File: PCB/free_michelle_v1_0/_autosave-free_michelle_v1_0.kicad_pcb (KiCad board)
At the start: 2 copper layers, 101 parts, among them J1 Zworka_TX, J10 ARK, J11 ARK, J12 Zworka_Buzzer, J13 ARK, J14 ARK, J15 Gniazdo 5VP DC 5,5x2,5, J16 Gniazdo 9V DC 5,5x2,5, J2 Zworka_RX, J3 GROVE_SW, J4 ARK, J5 ARK, J6 ARK, J7 ARK, J8 GROVE_SW, J9 A02YYUW_GroveCON, K1 FINDER-36.11, K2 FINDER-36.11, K3 FINDER-36.11, K4 FINDER-36.11, K5 FINDER-36.11, K6 FINDER-36.11, K7 FINDER-36.11, K8 FINDER-36.11, Q1 MMBT4403_PNP, Q2 MMBT4403_PNP, Q3 MMBT4403_PNP, Q4 MMBT4403_PNP, Q5 BSS138, Q6 MMBT4403_PNP, Q7 MMBT4403_PNP, Q8 MMBT4403_PNP, Q9 MMBT4403_PNP, SW1 Rotary_Encoder, SW2 SW_Push, SW3 SW_Push, U1 EEPROM_24AA01, U2 ESP8266_NodeMCU_v2, U3 DS3231M_RTC, U4 NRF24L01_Breakout, U5 BMP280, U6 LD1117V33, U7 L7805, U8 LD1117V33

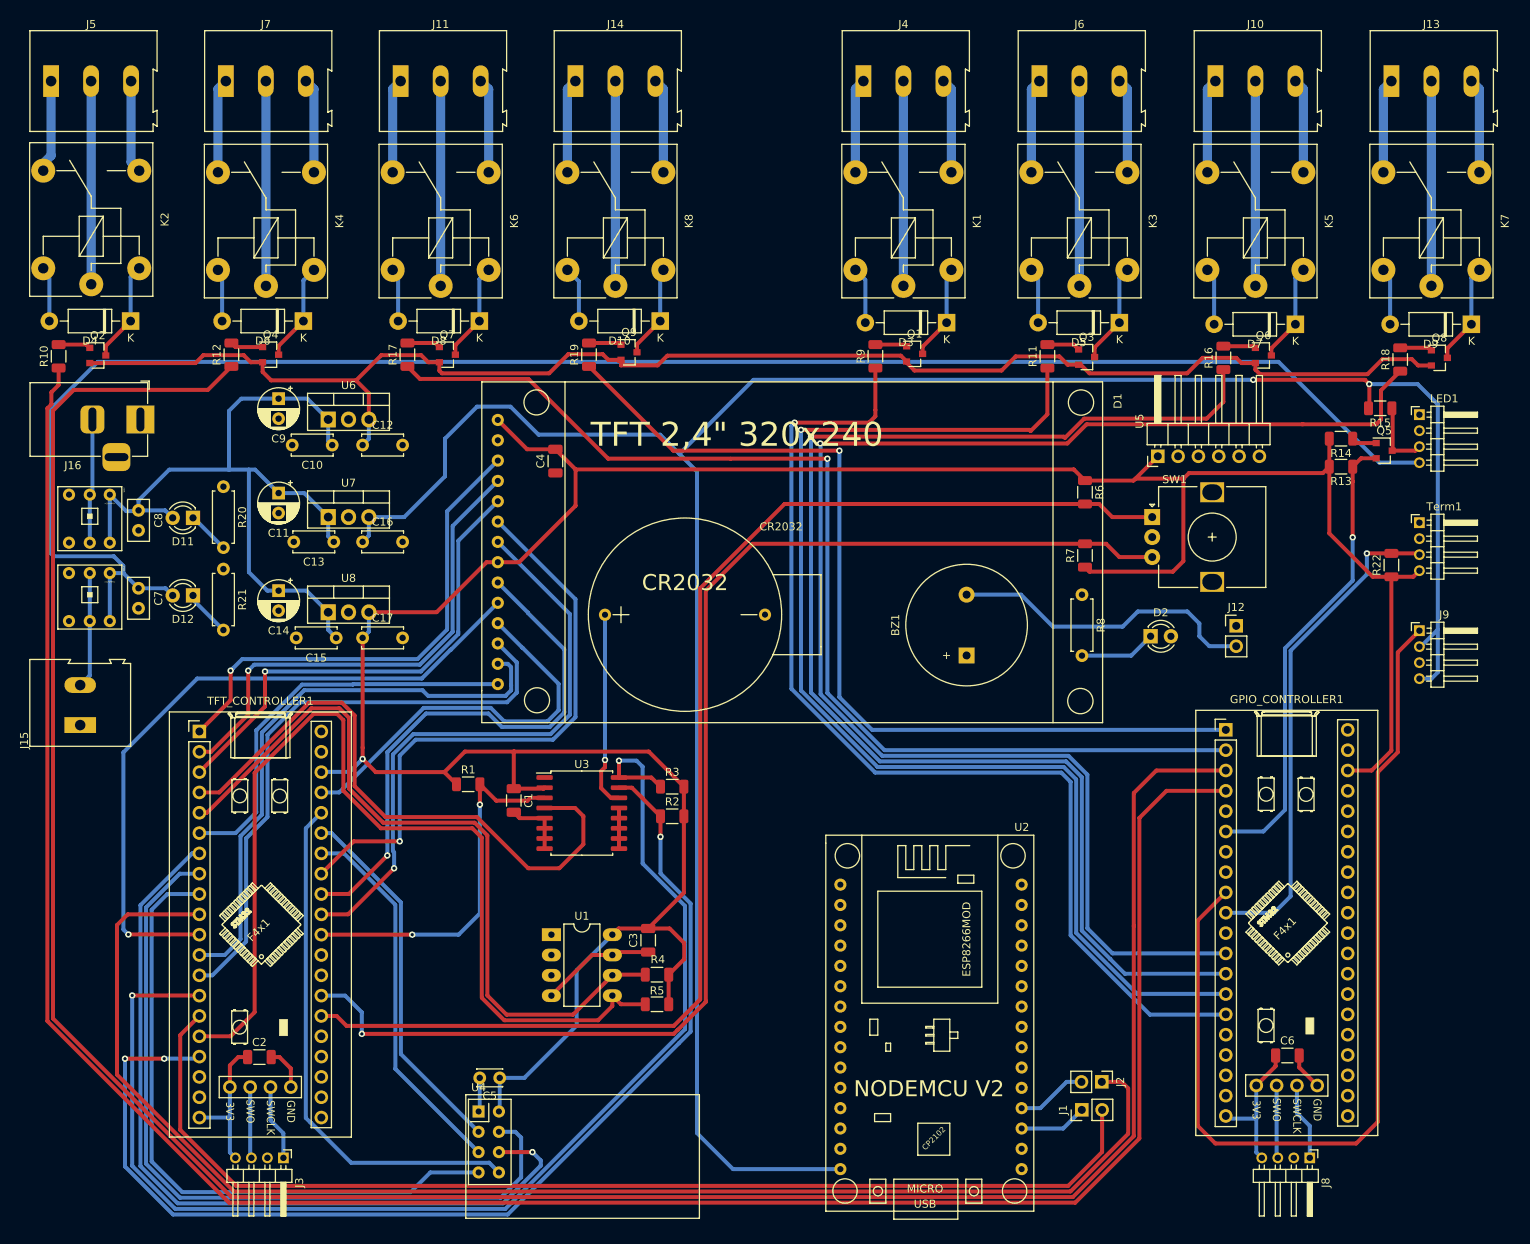
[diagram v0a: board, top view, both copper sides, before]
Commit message: Wykonane wszystkie polaczenia sygnalowe i zasilania, przed wylaniem masy
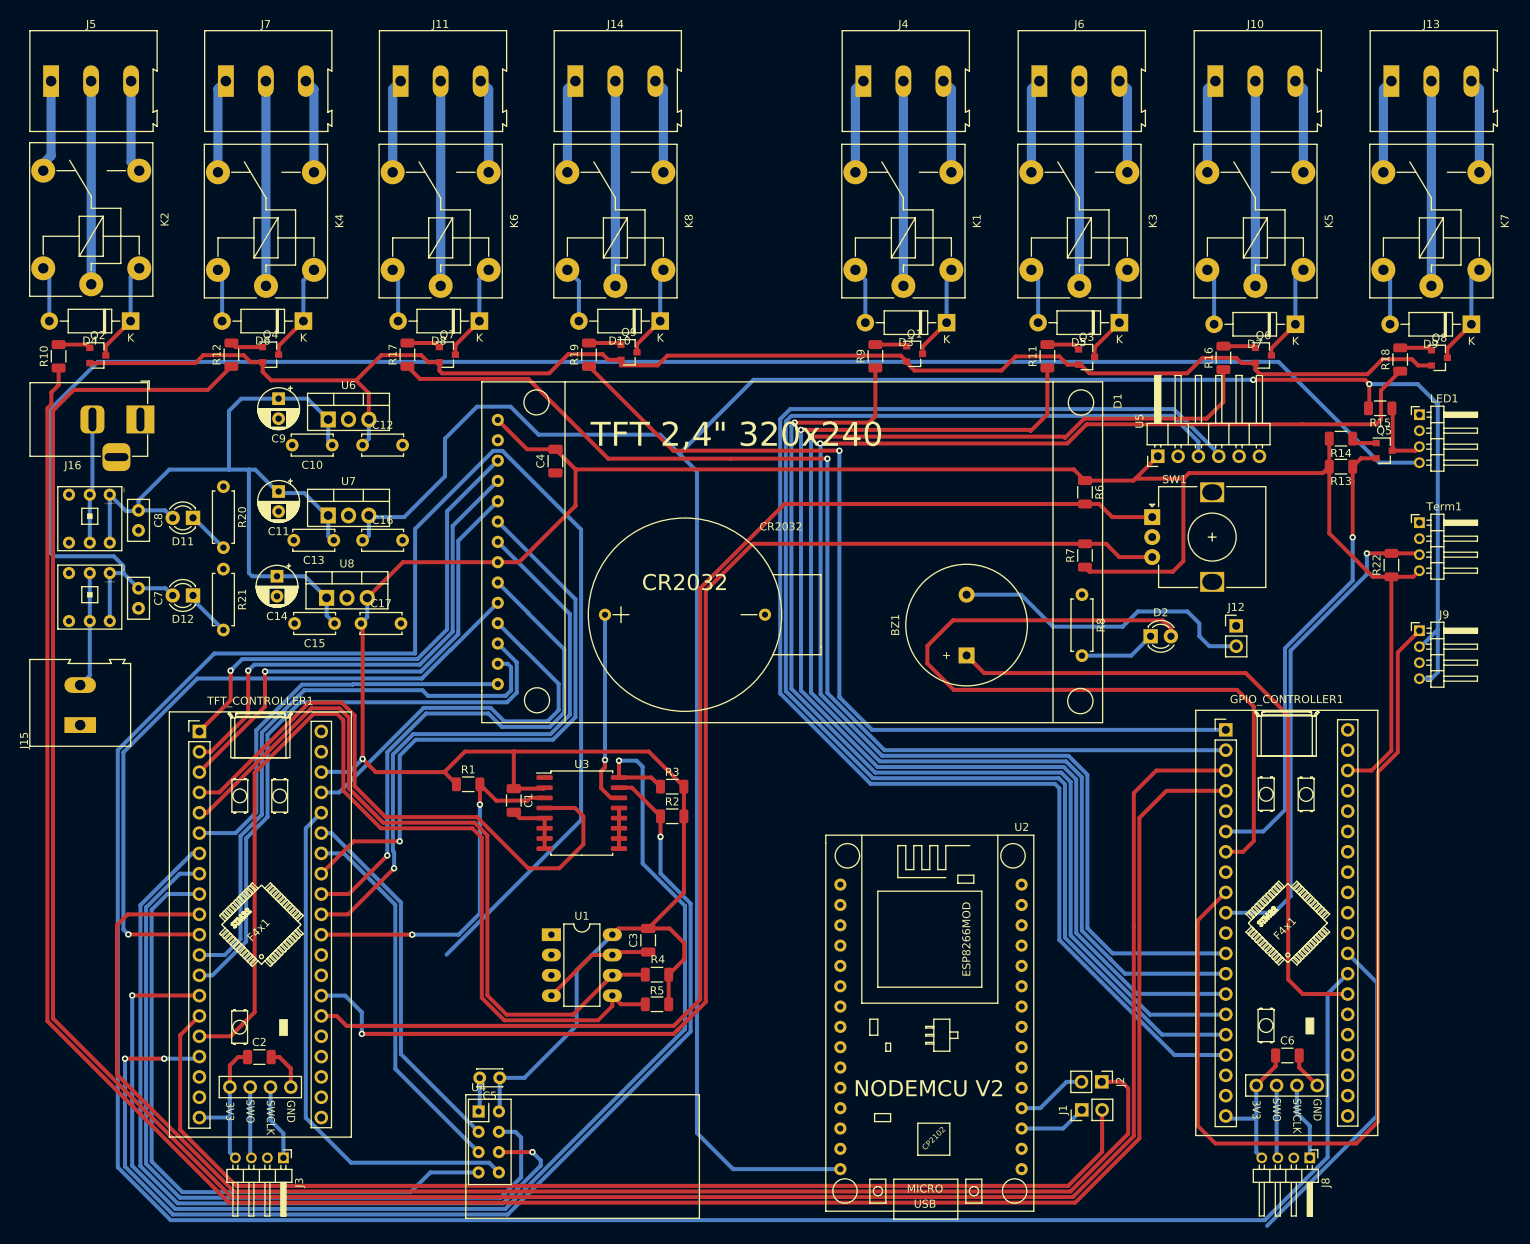
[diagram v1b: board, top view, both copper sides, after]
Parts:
- moved C14 1.81 mm to (56.2, 84.1)
- moved C15 1.81 mm to (63.4, 90.0)
- moved C17 1.81 mm to (66.7, 90.0)
- moved U8 1.81 mm to (62.4, 86.8)
- moved C11 0.20 mm to (56.4, 73.5)
- moved C13 0.20 mm to (63.3, 79.6)
- moved C16 0.20 mm to (66.9, 79.6)
- moved U7 0.20 mm to (62.6, 76.5)
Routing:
- net Net-(GPIO_CONTROLLER1-Pad8): track 0.00 -> 380.1 mm
- net BMP_SDA_PB9: track 0.00 -> 177.8 mm
- net BMP_SCL_PB8: track 0.00 -> 172.8 mm
- net USER_LED_PA10: track 0.00 -> 99.2 mm
- net Buzzer_PA1: track 0.00 -> 84.5 mm
- net Net-(GPIO_CONTROLLER1-Pad9): track 0.00 -> 41.3 mm
- net +3V3: track 408.5 -> 409.8 mm
- net +9V: track 100.8 -> 99.9 mm
